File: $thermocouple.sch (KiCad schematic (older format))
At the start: 61 parts, among them CON1 AVR-ISP-6, IC1 SP3485CN, IC2 ATMEGA88-A, P1 CONN_2, P2 CONN_4, U1 AD8237, U2 TC1047, U3 7805, U4 MCP6L01, X1 CRYSTAL

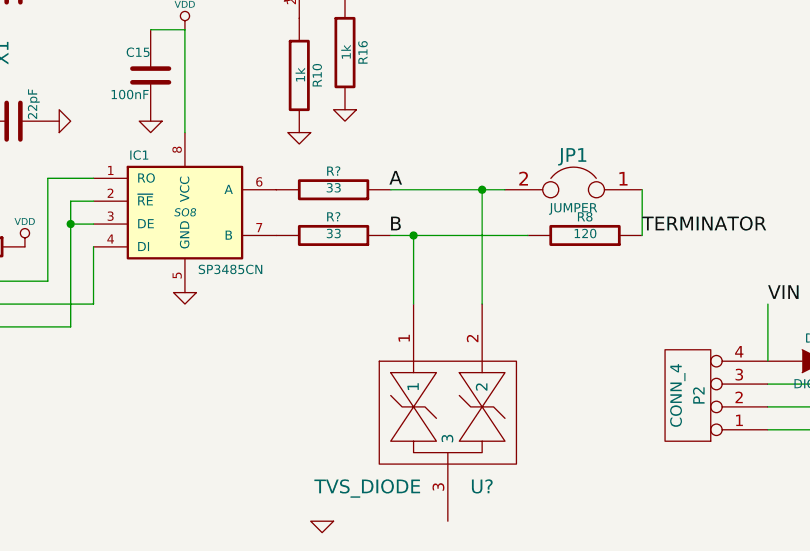
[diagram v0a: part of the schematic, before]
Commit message: RS485 protection added
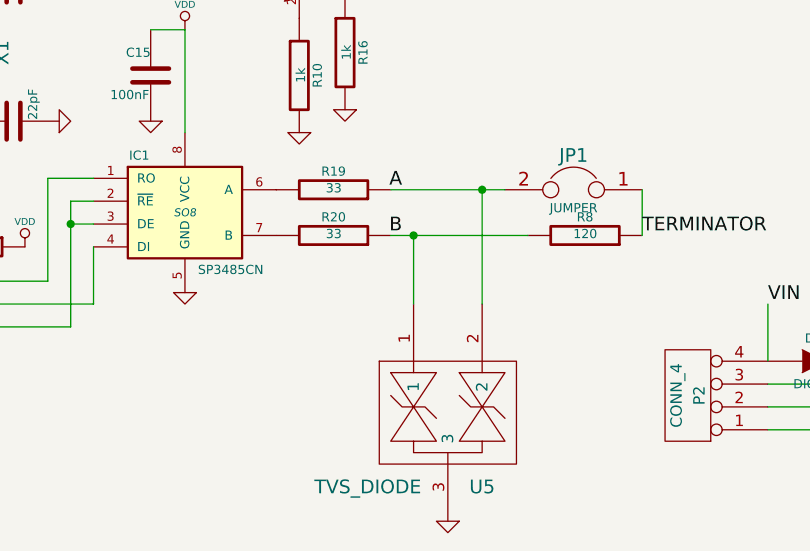
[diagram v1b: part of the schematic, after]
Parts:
- gave numbers to parts that had none: 3
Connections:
- net GND: now also U5.3
